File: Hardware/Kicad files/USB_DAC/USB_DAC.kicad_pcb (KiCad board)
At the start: 4 copper layers, 100 x 100 mm, 96 parts, among them IC1 ES9039Q2M, IC2 LT3094EDD_PBF, J1 NC3MAH, J10 B4B-PH-K-S, J3 B7B-PH-K-S, J5 Jack-DC, J6 Conn_ARM_JTAG_SWD_10, J7 B2B-PH-K-S, J8 NC3MAH, J9 USB4110GFA, U1 USB3300-EZK, U2 STM32H723ZGTx, U3 IP4234CZ6, U4 OPA1612AxD, U5 OPA1612AxD, U6 LT3042IMSE_PBF, U7 TPS7A2033PDBVR, Y3 NSC5083D

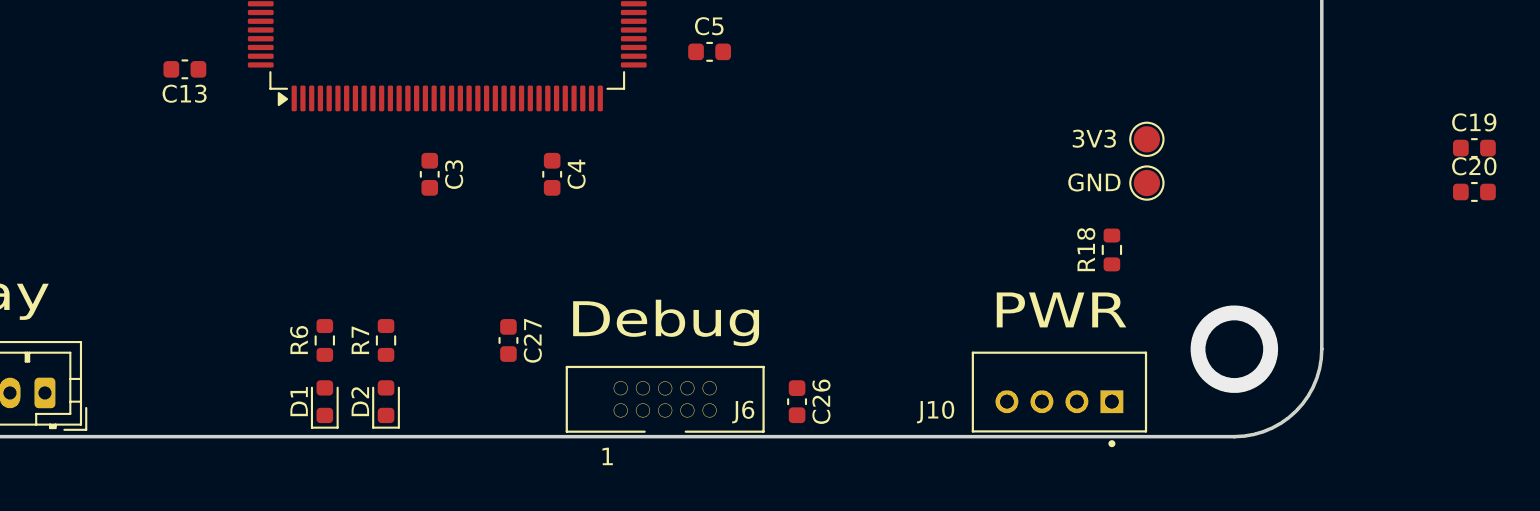
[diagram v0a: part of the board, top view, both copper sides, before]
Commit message: added STM code files and modified PCB
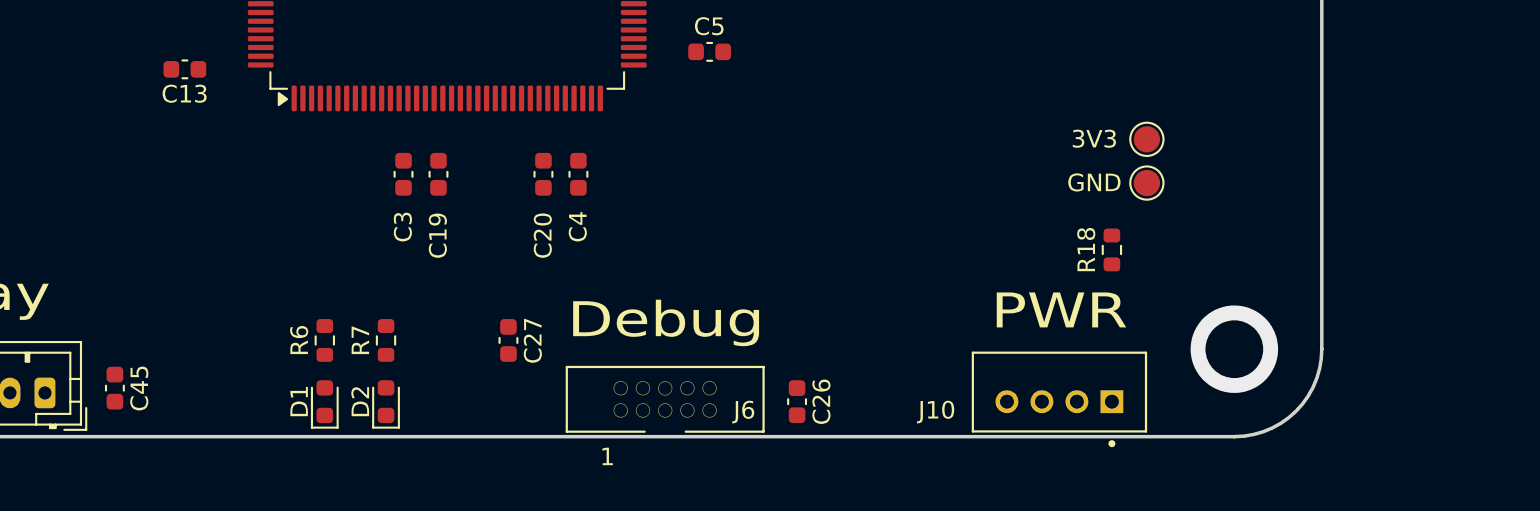
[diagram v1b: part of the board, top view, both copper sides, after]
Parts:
- added C45: 100n, Capacitor_SMD:C_0603_1608Metric, F.Cu at (131.0, 147.2)
- R16, R17: value R -> 47k
- moved C19 59.2 mm to (149.5, 135.0), turned to -90 degrees
- moved C20 53.2 mm to (155.5, 135.0), turned to -90 degrees
- moved C3 1.50 mm to (147.5, 135.0)
- moved C4 1.50 mm to (157.5, 135.0)
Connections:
- J3 pad 1: unconnected-(J3-Pad1) -> +3V3
- J3 pad 2: unconnected-(J3-Pad2) -> GND
- J3 pad 3: unconnected-(J3-Pad3) -> SPI_MOSI
- J3 pad 4: unconnected-(J3-Pad4) -> SPI_SCK
- J3 pad 5: unconnected-(J3-Pad5) -> SPI_CS
- J3 pad 6: unconnected-(J3-Pad6) -> DISPLAY_DC
- J3 pad 7: unconnected-(J3-Pad7) -> DISPLAY_RST
- U2 pad 1: unconnected-(U2-PE2-Pad1) -> SPI_SCK
- U2 pad 111: unconnected-(U2-PC10-Pad111) -> SDA
- U2 pad 112: unconnected-(U2-PC11-Pad112) -> SCL
- U2 pad 141: unconnected-(U2-PE0-Pad141) -> DISPLAY_DC
- U2 pad 142: unconnected-(U2-PE1-Pad142) -> DISPLAY_RST
- U2 pad 2: unconnected-(U2-PE3-Pad2) -> SPI_CS
- U2 pad 23: unconnected-(U2-PH0-Pad23) -> /MCU/OSC_IN
- U2 pad 24: unconnected-(U2-PH1-Pad24) -> /MCU/OSC_OUT
- U2 pad 5: unconnected-(U2-PE6-Pad5) -> SPI_MOSI
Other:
- board text added: "3V3"
- board text added: "CS"
- board text added: "DC"
- board text added: "MOSI"
- board text added: "RST"
- board text added: "SCK"

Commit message: Updated PCB and schematics
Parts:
- added C46: 1u, Capacitor_SMD:C_0603_1608Metric, F.Cu at (192.1, 122.0)
- added C47: 1u, Capacitor_SMD:C_0603_1608Metric, F.Cu at (192.1, 115.0)
- added C48: 1u, Capacitor_SMD:C_0603_1608Metric, F.Cu at (192.1, 124.0)
- added R27: 10k, Resistor_SMD:R_0603_1608Metric, F.Cu at (186.0, 138.2)
- added U8: TPS7A2033PDBVR, TPS7A2033PDBVR:SOT95P280X145-5N, F.Cu at (192.1, 118.5)
- added U9: MAX6816EUS_T, MAX6816EUS_T:SOT192P237X122-4N, F.Cu at (183.0, 137.8)
- added Y1: C5S-20.000-12-3030-X-R, C5S-20.000-12-3030-X-R:XTAL_C5S-20.000-12-3030-X-R, F.Cu at (152.5, 136.0)
- added Y4: C5S-20.000-12-3030-X-R, C5S-20.000-12-3030-X-R:XTAL_C5S-20.000-12-3030-X-R, F.Cu at (176.4, 130.4)
- moved C26 46.8 mm to (123.2, 145.5)
- moved J6 46.5 mm to (116.0, 147.6)
- moved C27 28.3 mm to (125.2, 145.5)
- moved R3 25.7 mm to (176.4, 137.4), turned to 0 degrees
- moved C25 21.3 mm to (178.2, 134.2)
- moved C24 20.9 mm to (174.7, 134.2), turned to 180 degrees
- moved R2 18.4 mm to (184.8, 129.7), turned to -90 degrees
- moved C45 18.1 mm to (149.0, 145.2)
- moved J3 18.0 mm to (145.0, 147.8)
- moved C21 16.4 mm to (184.0, 125.9), turned to 180 degrees
- moved C31 16.2 mm to (182.8, 129.7), turned to -90 degrees
- moved R1 15.4 mm to (184.0, 123.9), turned to 180 degrees
- moved C23 15.1 mm to (172.0, 129.8), turned to -90 degrees
- moved C28 14.8 mm to (184.0, 121.9), turned to 0 degrees
- moved C22 14.2 mm to (180.8, 129.7), turned to -90 degrees
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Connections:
- 3V3 pad 1: (no net) -> +3V3
- C16 pad 1: Net-(PS1-+VIN_(VCC)) -> DC_IN
- C17 pad 1: Net-(PS1-+VIN_(VCC)) -> DC_IN
- C19 pad 2: Net-(C19-Pad2) -> GND
- C20 pad 2: Net-(C19-Pad2) -> GND
- C33 pad 1: Net-(PS1-+VIN_(VCC)) -> DC_IN
- GND pad 1: (no net) -> GND
- J6 pad 1: unconnected-(J6-VTref-Pad1) -> +3V3
- J7 pad 1: Net-(J7-Pad1) -> DC_IN
- J7 pad 2: Net-(J7-Pad1) -> GND
- PS1 pad 2: Net-(PS1-+VIN_(VCC)) -> DC_IN
- U2 pad 141: DISPLAY_DC -> DISPLAY_RST
- U2 pad 142: DISPLAY_RST -> DISPLAY_DC
- U2 pad 8: unconnected-(U2-PC14-Pad8) -> ACT_LED
- U2 pad 9: unconnected-(U2-PC15-Pad9) -> ERR_LED
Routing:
- net GND: track 0.00 -> 87.2 mm, vias 4 -> 66
- net USB_VBUS: track 0.00 -> 86.6 mm, vias 0 -> 2
- net +3V3: track 0.00 -> 65.5 mm, vias 0 -> 22
- net SWD_JTMS: track 0.00 -> 61.2 mm, vias 0 -> 2
- net SWD_JTCK: track 0.00 -> 54.9 mm, vias 0 -> 2
- net SWD_JTDI: track 0.00 -> 51.9 mm, vias 0 -> 2
- net I2S2_SDO: track 0.00 -> 43.4 mm, vias 0 -> 2
- net SWD_JTDO: track 0.00 -> 42.1 mm
- net DATA4: track 0.00 -> 39.9 mm
- net DATA3: track 0.00 -> 39.7 mm
- net DATA1: track 0.00 -> 39.7 mm
- net DATA2: track 0.00 -> 39.7 mm
- net DATA5: track 0.00 -> 39.7 mm
- net ULPI_NXT: track 0.00 -> 39.5 mm, vias 0 -> 2
- net SWD_NJTRST: track 0.00 -> 39.4 mm
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- added copper zone on In2.Cu, net +3V3
- added copper zone on F.Cu, net DC_IN
- added copper zone on In1.Cu, net GND
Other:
- board text removed: "PWR"

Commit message: Updated PCB and schematics
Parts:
- added BOOT: TestPoint_Pad_D1.5mm, TestPoint:TestPoint_Pad_D1.5mm, F.Cu at (123.0, 137.0)
- added C49: 1u, Capacitor_SMD:C_0603_1608Metric, F.Cu at (193.2, 106.5)
- added C50: 1u, Capacitor_SMD:C_0603_1608Metric, F.Cu at (193.2, 104.5)
- added C51: 1u, Capacitor_SMD:C_0603_1608Metric, F.Cu at (193.2, 116.0)
- added C52: 1u, Capacitor_SMD:C_0603_1608Metric, F.Cu at (193.2, 118.0)
- added C53: 4u7, Capacitor_SMD:C_1206_3216Metric, F.Cu at (161.0, 84.8)
- added C54: 4u7, Capacitor_SMD:C_1206_3216Metric, F.Cu at (165.2, 87.3)
- added C55: 4u7, Capacitor_SMD:C_1206_3216Metric, F.Cu at (171.0, 85.8)
- added C56: 4u7, Capacitor_SMD:C_1206_3216Metric, F.Cu at (161.0, 74.3)
- added C57: 4u7, Capacitor_SMD:C_1206_3216Metric, F.Cu at (171.0, 76.1)
- added C58: 4u7, Capacitor_SMD:C_1206_3216Metric, F.Cu at (165.2, 77.6)
- added C59: 100n, Capacitor_SMD:C_0603_1608Metric, F.Cu at (146.5, 100.0)
- added C60: 100n, Capacitor_SMD:C_0603_1608Metric, F.Cu at (139.2, 100.0)
- added R28: 10k, Resistor_SMD:R_0603_1608Metric, F.Cu at (135.0, 132.8)
- added R29: 90k 1%, Resistor_SMD:R_0603_1608Metric, F.Cu at (158.8, 84.8)
- added R30: 90k 1%, Resistor_SMD:R_0603_1608Metric, F.Cu at (158.8, 74.3)
- added RST: TestPoint_Pad_D1.5mm, TestPoint:TestPoint_Pad_D1.5mm, F.Cu at (123.0, 139.8)
- added U10: LM1117MP-5.0, Package_TO_SOT_SMD:SOT-223-3_TabPin2, F.Cu at (192.8, 111.2)
- moved C27 22.0 mm to (135.0, 125.8), turned to 180 degrees
- moved C26 18.9 mm to (135.0, 130.8), turned to 180 degrees
- moved R20 18.0 mm to (127.0, 81.5)
- moved R19 14.0 mm to (125.0, 81.5)
- moved C42 10.0 mm to (123.0, 81.5)
- moved 3V3 7.75 mm to (195.8, 136.8)
- moved C46 7.75 mm to (192.1, 129.8)
- moved C47 7.75 mm to (192.1, 122.8)
- moved C48 7.75 mm to (192.1, 131.8)
- moved GND 7.75 mm to (195.8, 139.3)
- moved U8 7.75 mm to (192.1, 126.2)
- moved IC2 6.30 mm to (166.1, 73.7), turned to 180 degrees
- moved U6 3.83 mm to (166.1, 83.8), turned to 180 degrees
- moved U7 1.78 mm to (142.8, 100.0), turned to 180 degrees
- moved C29 1.68 mm to (174.5, 118.2)
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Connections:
- C14 pad 1: +12VA -> +12V
- C14 pad 2: GNDA -> GND
- C15 pad 1: GNDA -> GND
- C15 pad 2: -12VA -> -12V
- C18 pad 1: +12VA -> +12V
- C18 pad 2: GNDA -> GND
- C32 pad 1: GNDA -> GND
- C32 pad 2: -12VA -> -12V
- C37 pad 1: GNDA -> GND
- C38 pad 2: GNDA -> GND
- C39 pad 1: GNDA -> GND
- C40 pad 1: GNDA -> GND
- C41 pad 2: GNDA -> GND
- IC1 pad 11: GNDA -> GND
- IC1 pad 17: GNDA -> GND
- IC1 pad 19: GNDA -> GND
- IC1 pad 20: GNDA -> GND
- IC1 pad 29: GNDA -> GND
- IC1 pad 30: GNDA -> GND
- IC1 pad 33: GNDA -> GND
- IC2 pad 1: unconnected-(IC2-IN_1-Pad1) -> -12V
- IC2 pad 10: unconnected-(IC2-OUTS-Pad10) -> -9VA
- IC2 pad 11: unconnected-(IC2-OUT_1-Pad11) -> -9VA
- IC2 pad 12: unconnected-(IC2-OUT_2-Pad12) -> -9VA
- IC2 pad 2: unconnected-(IC2-IN_2-Pad2) -> -12V
- IC2 pad 3: unconnected-(IC2-EN/UV-Pad3) -> -12V
- IC2 pad 5: unconnected-(IC2-PGFB-Pad5) -> -12V
- IC2 pad 6: unconnected-(IC2-ILIM-Pad6) -> GND
- IC2 pad 8: unconnected-(IC2-SET-Pad8) -> Net-(IC2-SET)
- IC2 pad 9: unconnected-(IC2-GND-Pad9) -> GND
- PS1 pad 6: +12VA -> +12V
- PS1 pad 7: GNDA -> GND
- PS1 pad 8: -12VA -> -12V
- U2 pad 35: unconnected-(U2-PA1-Pad35) -> BTN_MCU
- U2 pad 36: unconnected-(U2-PA2-Pad36) -> BTN_LED
- U4 pad 3: GNDA -> GND
- U5 pad 3: GNDA -> GND
- U6 pad 1: Net-(U6-IN-Pad1) -> +12V
- U6 pad 10: unconnected-(U6-OUT-Pad10) -> +9VA
- U6 pad 2: Net-(U6-IN-Pad1) -> +12V
- U6 pad 3: unconnected-(U6-EN/UV-Pad3) -> +12V
- U6 pad 5: unconnected-(U6-ILIM-Pad5) -> GND
- U6 pad 6: unconnected-(U6-PGFB-Pad6) -> +12V
- U6 pad 7: unconnected-(U6-SET-Pad7) -> Net-(U6-SET)
- U6 pad 9: unconnected-(U6-OUTS-Pad9) -> +9VA
- U7 pad 1: unconnected-(U7-IN-Pad1) -> +9VA
- U7 pad 2: unconnected-(U7-GND-Pad2) -> GND
- U7 pad 3: unconnected-(U7-EN-Pad3) -> +9VA
- U7 pad 5: unconnected-(U7-OUT-Pad5) -> +3.3VA
- Y3 pad 2: GNDA -> GND
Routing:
- net Net-(RST1A-D): track 0.00 -> 44.1 mm, vias 0 -> 3
- net DATA0: track 0.00 -> 40.8 mm
- net BTN_LED: track 0.00 -> 40.6 mm
- net BTN_MCU: track 0.00 -> 36.8 mm
- net DAC2: track 0.00 -> 28.4 mm, vias 0 -> 4
- net DAC2B: track 0.00 -> 24.6 mm, vias 0 -> 2
- net GND: track 87.2 -> 111.0 mm, vias 66 -> 84
- net Net-(BOOT1A-D): track 0.00 -> 22.2 mm
- net Net-(C43-Pad2): track 1.81 -> 23.0 mm
- net +5V: track 5.35 -> 16.2 mm
- net Net-(C42-Pad2): track 7.62 -> 14.8 mm
- net +3V3: track 65.5 -> 67.9 mm, vias 22 -> 24
- net +3.3VA: track 22.4 -> 24.6 mm, vias 0 -> 4
- net ULPI_CK: track 35.7 -> 37.7 mm
- net DATA6: track 39.1 -> 40.7 mm
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- added copper zone on In2.Cu, net +3.3VA
